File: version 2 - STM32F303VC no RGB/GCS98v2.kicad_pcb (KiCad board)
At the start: 2 copper layers, 201 parts, among them SW1 SW_Push, SW2 SW_Push_SPDT, U1 STM32F303CCTx

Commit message: columns routed
updating graphics driver fixed the corruption issue
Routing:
- net col17: track 92.0 -> 305.0 mm
- net col16: track 100.3 -> 291.7 mm, vias 0 -> 2
- net col15: track 79.1 -> 251.9 mm
- net col12: track 46.7 -> 215.8 mm
- net col14: track 101.6 -> 254.9 mm, vias 0 -> 2
- net col00: track 110.0 -> 246.1 mm
- net col13: track 112.0 -> 243.0 mm, vias 0 -> 2
- net col01: track 117.6 -> 229.5 mm
- net col11: track 120.6 -> 223.7 mm, vias 0 -> 2
- net col02: track 114.0 -> 201.3 mm
- net col10: track 117.5 -> 195.6 mm, vias 0 -> 2
- net col03: track 88.6 -> 152.0 mm
- net col09: track 114.5 -> 175.7 mm, vias 0 -> 2
- net col04: track 90.6 -> 135.6 mm
- net col08: track 88.6 -> 133.0 mm
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
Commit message: column traces inverted to back copper
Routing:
- net row2: track 325.2 -> 344.2 mm
- net col02: track 201.3 -> 199.0 mm
- net col00: track 246.1 -> 244.1 mm
- net col01: track 229.5 -> 228.6 mm
- net row5: vias 0 -> 2
- net col16: vias 2 -> 1
- net col13: vias 2 -> 1
- net col14: vias 2 -> 1
- net col11: vias 2 -> 1
- net col09: vias 2 -> 1
- net col12: vias 0 -> 1
- net col10: vias 2 -> 1

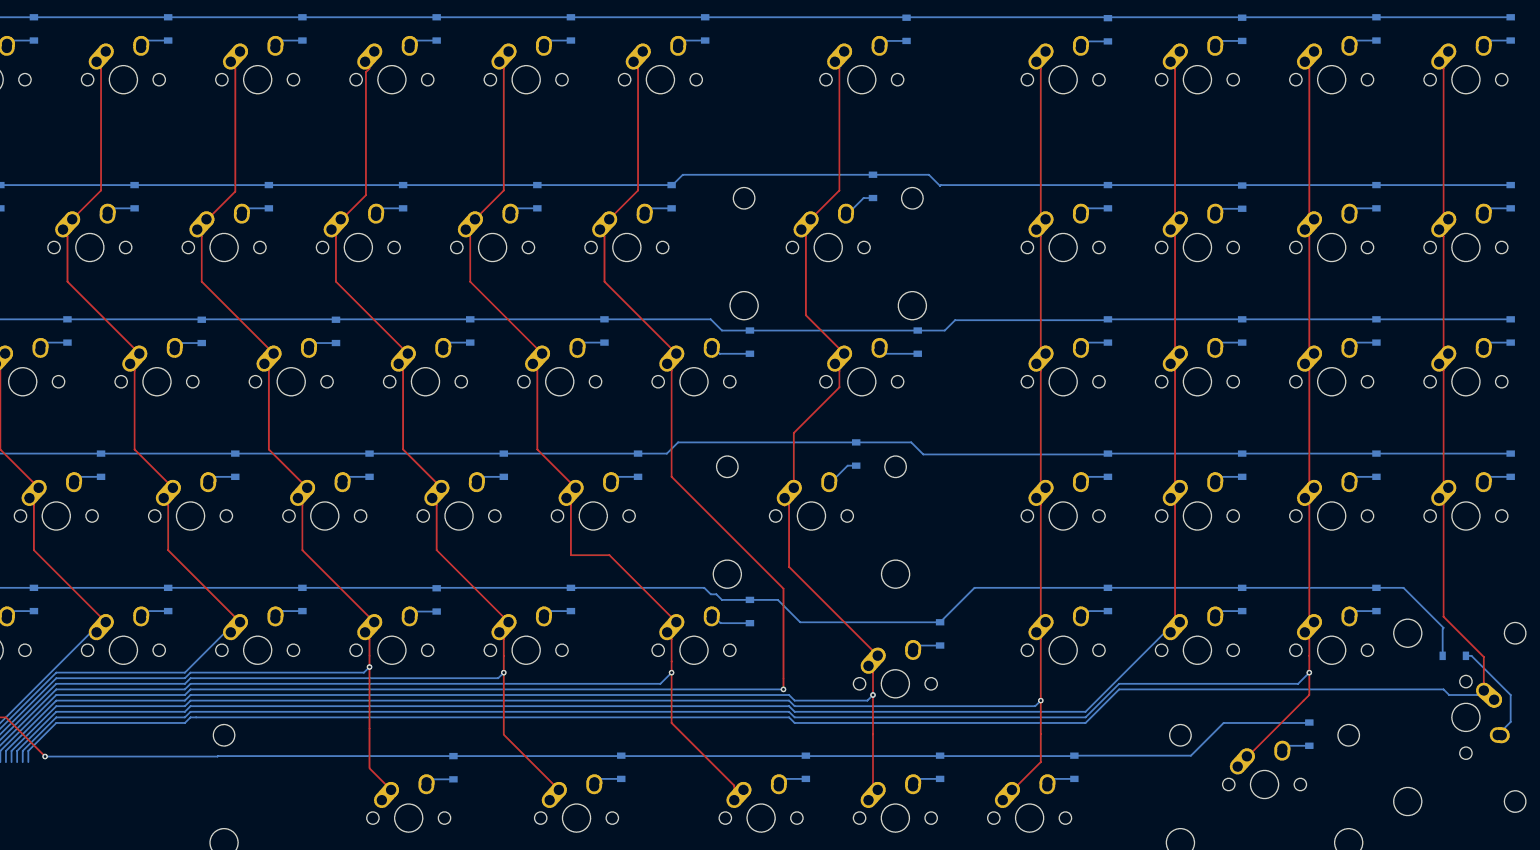
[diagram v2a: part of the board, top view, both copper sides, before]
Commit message: rows and columns fully routed to spacebar area
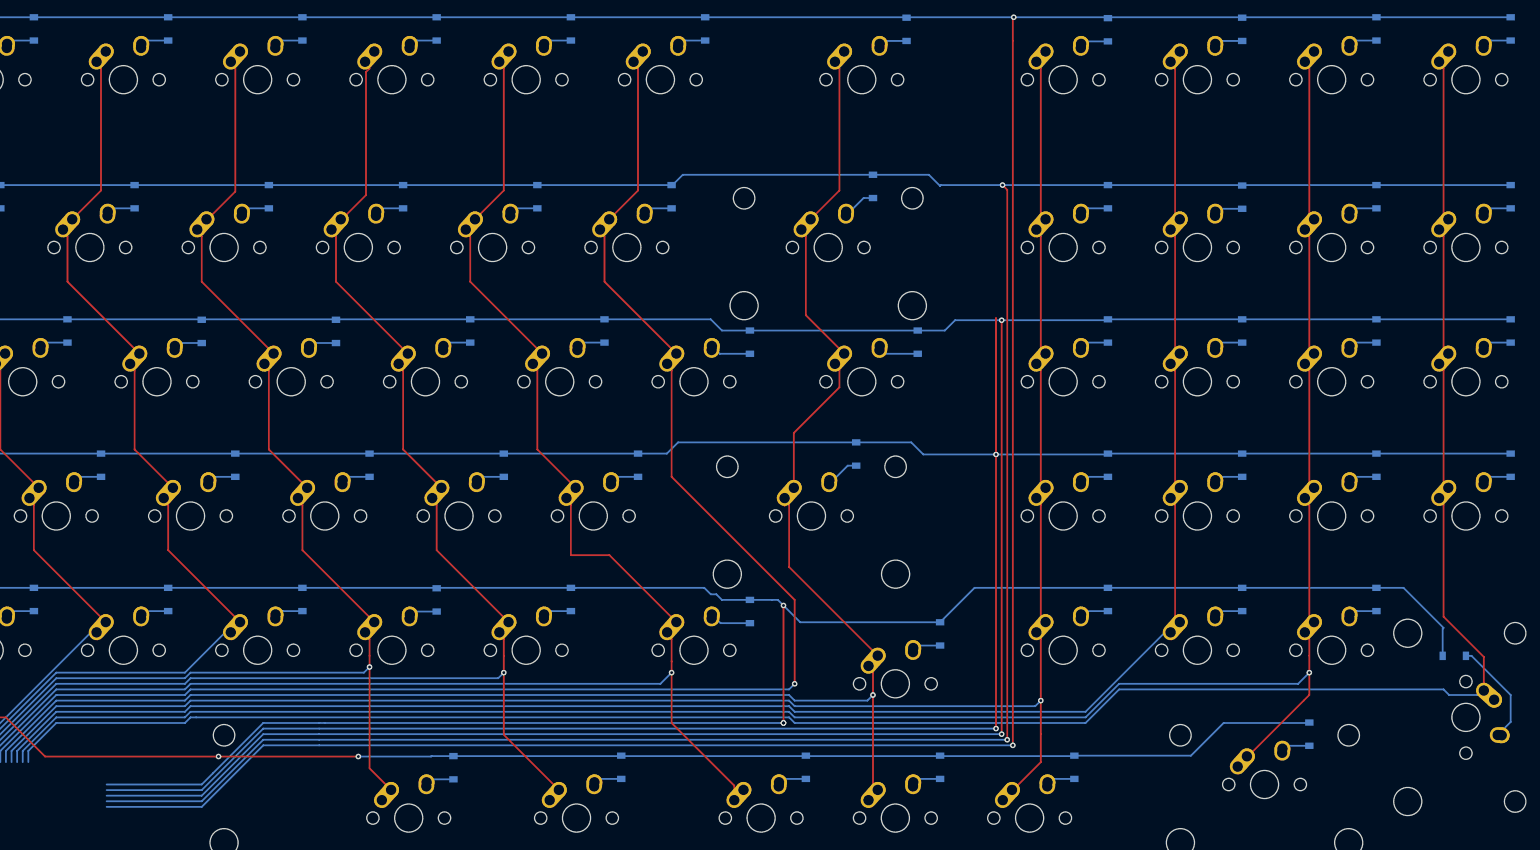
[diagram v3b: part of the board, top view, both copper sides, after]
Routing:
- net row0: track 347.7 -> 583.3 mm, vias 0 -> 2
- net row1: track 349.0 -> 559.4 mm, vias 0 -> 2
- net row3: track 341.9 -> 549.3 mm, vias 0 -> 2
- net row2: track 344.2 -> 533.6 mm, vias 0 -> 2
- net row4: track 338.3 -> 454.6 mm, vias 0 -> 3
- net col12: track 215.8 -> 217.5 mm
- net row5: vias 2 -> 3

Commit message: added TODO for when I pick this back up
signing off for the night
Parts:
- moved U1 37.7 mm to (261.3, 344.1)
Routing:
- net row5: track 324.0 -> 341.7 mm
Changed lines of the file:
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@@
     (thickness 1.6)
     (drawings 588)
-    (tracks 819)
+    (tracks 822)
     (zones 0)
     (modules 201)
@@
   )
   (module Package_QFP:LQFP-48_7x7mm_P0.5mm (layer B.Cu)
-    (at 243.1625 377.0675)
+    (at 261.3375 344.0625)
     (descr "LQFP, 48 Pin (https://www.analog.com/media/en/technical-documentation/data-sheets/ltc2358-16.pdf), generated with kicad-footprint-generator ipc_gullwing_generator.py")
     (tags "LQFP QFP")
@@
   (segment (start 323.85 335.75625) (end 323.9125 335.69375) (width 0.254) (layer B.Cu) (net 97))
   (segment (start 313.53125 335.75625) (end 323.85 335.75625) (width 0.254) (layer B.Cu) (net 97))
+  (segment (start 293.6875 335.75625) (end 293.6875 336.55) (width 0.254) (layer B.Cu) (net 97))
+  (segment (start 293.6875 336.55) (end 291.30625 338.93125) (width 0.254) (layer B.Cu) (net 97))
+  (segment (start 291.30625 338.93125) (end 277.8125 338.93125) (width 0.254) (layer B.Cu) (net 97))
   (segment (start 258.7625 334.9625) (end 258.7625 336.55) (width 0.254) (layer B.Cu) (net 114))
   (segment (start 275.59 318.135) (end 258.7625 334.9625) (width 0.254) (layer B.Cu) (net 114))
